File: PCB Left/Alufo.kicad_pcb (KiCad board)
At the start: 2 copper layers, 282.6 x 90.9 mm, 93 parts, among them J1 USB_C_Receptacle_USB2.0_16P_2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, J3 USB_C_Receptacle_USB2.0_16P_2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, J5 Shield_Connection, J7 Shield_Connection, K11 PG1350, K12 PG1350, K13 PG1350, K14 PG1350, K15 PG1350, K16 PG1350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

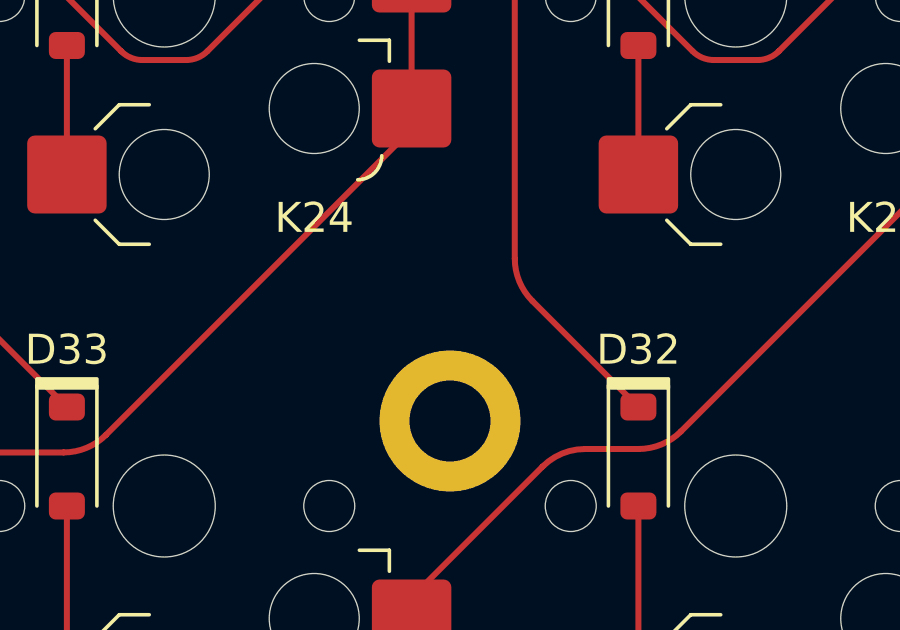
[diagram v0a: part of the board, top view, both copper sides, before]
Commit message: Add shield connection to H3 (lower middle mounting hole)
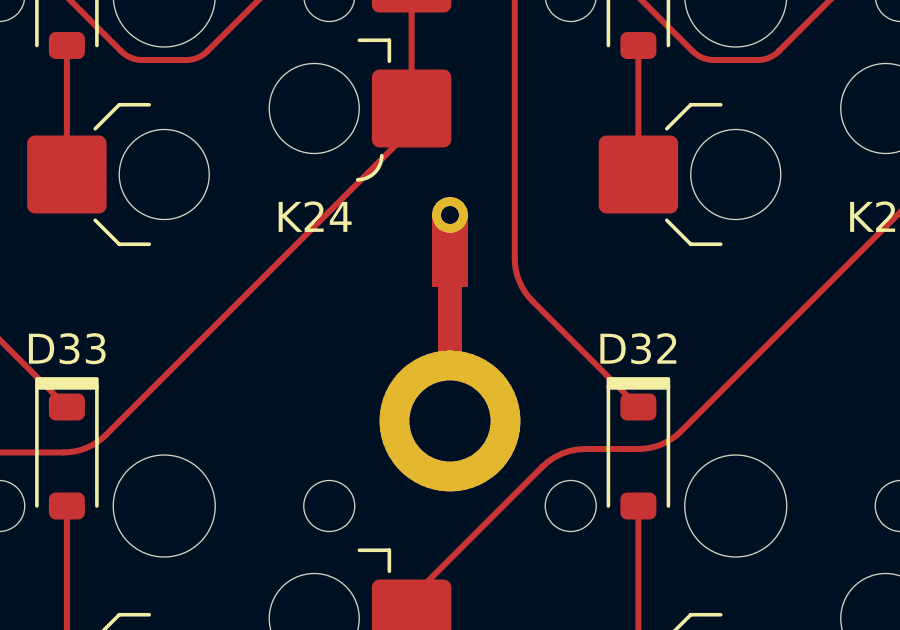
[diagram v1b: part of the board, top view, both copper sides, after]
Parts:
- added J9: Shield_Connection, Project_Library:Shield_Connector, F.Cu at (238.1, 64.9)
- H3: footprint Project_Library:MountingHole_2.2mm_M2_SMD_Solder_Nut -> Project_Library:MountingHole_2.2mm_M2_SMD_Solder_Nut_Pad
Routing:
- net Net-(J9-Pin_1): track 0.00 -> 5.67 mm
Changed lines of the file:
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@@
 	(net 68 "unconnected-(J3-SHIELD-PadS3)")
 	(net 69 "VCC'")
+	(net 70 "Net-(J9-Pin_1)")
 	(footprint "Project_Library:SW_choc_v1_HS_CPG135001S30_1layer_1u"
 		(layer "F.Cu")
@@
 		)
 	)
-	(footprint "Project_Library:MountingHole_2.2mm_M2_SMD_Solder_Nut"
+	(footprint "Project_Library:MountingHole_2.2mm_M2_SMD_Solder_Nut_Pad"
 		(layer "F.Cu")
 		(at 238.125 70.83335)
@@
 			)
 		)
-		(property "Description" "Mounting Hole without connection"
+		(property "Description" "Mounting Hole with connection"
 			(at 0 0 0)
 			(unlocked yes)
@@
 			)
 		)
-		(property ki_fp_filters "MountingHole*")
+		(property ki_fp_filters "MountingHole*Pad*")
 		(sheetname "/")
 		(sheetfile "Alufo.kicad_sch")
@@
 		(fp_circle
 			(center 0 0)
-			(end 3.35 0)
+			(end 2.5 0)
 			(stroke
 				(width 0.1)
@@
 			)
 		)
-		(pad "" thru_hole circle
+		(pad "1" thru_hole circle
 			(at 0 0)
 			(size 4.7 4.7)
@@
 			(layers "*.Cu" "F.Mask")
 			(remove_unused_layers no)
+			(net 70 "Net-(J9-Pin_1)")
+			(pinfunction "1")
+			(pintype "input")
 		)
 		(embedded_fonts no)
@@
 		(embedded_fonts no)
 	)
+	(footprint "Project_Library:Shield_Connector"
+		(layer "F.Cu")
+		(at 238.125 64.866682 180)
+		(descr "Wire connection from PCB to aluminum core")
+		(property "Reference" "J9"
+			(at 0 -0.499999 180)
+			(unlocked yes)
+			(layer "F.SilkS")
+			(hide yes)
+			(effects
+				(font
+					(size 1 1)
+					(thickness 0.1)
+				)
+			)
+		)
+		(property "Value" "Shield_Connection"
+			(at 0 1 180)
+			(unlocked yes)
+			(layer "F.Fab")
+			(effects
+				(font
+					(size 1 1)
+					(thickness 0.15)
+				)
+			)
+		)
+		(property "Datasheet" ""
+			(at 0 0 180)
+			(unlocked yes)
+			(layer "F.Fab")
+			(hide yes)
+			(effects
+				(font
+					(size 1 1)
+					(thickness 0.15)
+				)
+			)
+		)
+		(property "Description" "Generic connector, single row, 01x01, script generated (kicad-library-utils/schlib/autogen/connector/)"
+			(at 0 0 180)
+			(unlocked yes)
+			(layer "F.Fab")
+			(hide yes)
+			(effects
+				(font
+					(size 1 1)
+					(thickness 0.15)
+				)
+			)
+		)
+		(property ki_fp_filters "Connector*:*_1x??_*")
+		(sheetname "/")
+		(sheetfile "Alufo.kicad_sch")
+		(attr smd)
+		(fp_poly
+			(pts
+				(arc
+					(start -0.4 -1.8)
+					(mid -0.753553 -1.653553)
+					(end -0.9 -1.3)
+				)
+				(arc
+					(start -0.9 0.9)
+					(mid -0.636396 1.536396)
+					(end 0 1.8)
+				)
+				(arc
+					(start 0 1.8)
+					(mid 0.636396 1.536396)
+					(end 0.9 0.9)
+				)
+				(arc
+					(start 0.9 -1.3)
+					(mid 0.753553 -1.653553)
+					(end 0.4 -1.8)
+				)
+			)
+			(stroke
+				(width 0.1)
+				(type solid)
+			)
+			(fill no)
+			(layer "User.3")
+		)
+		(fp_text user "${REFERENCE}"
+			(at 0 2.5 180)
+			(unlocked yes)
+			(layer "F.Fab")
+			(effects
+				(font
+					(size 1 1)
+					(thickness 0.15)
+				)
+			)
+		)
+		(pad "1" smd roundrect
+			(at 0 -0.3 180)
+			(size 1.2 2.4)
+			(layers "F.Cu" "F.Mask" "F.Paste")
+			(roundrect_rratio 0.2)
+			(chamfer_ratio 0)
+			(chamfer bottom_left bottom_right)
+			(net 70 "Net-(J9-Pin_1)")
+			(pinfunction "Pin_1")
+			(pintype "passive")
+			(thermal_bridge_angle 45)
+		)
+		(pad "1" thru_hole circle
+			(at 0 0.9 180)
+			(size 1.2 1.2)
+			(drill 0.6)
+			(layers "*.Cu" "*.Paste" "*.Mask")
+			(remove_unused_layers no)
+			(net 70 "Net-(J9-Pin_1)")
+			(pinfunction "Pin_1")
+			(pintype "passive")
+		)
+		(embedded_fonts no)
+	)
 	(footprint "BGK_Kicad:D_SOD-323"
 		(layer "F.Cu")
@@
 		(net 69)
 	)
+	(segment
+		(start 238.125 65.166682)
+		(end 238.125 70.83335)
+		(width 0.8)
+		(layer "F.Cu")
+		(net 70)
+	)
 	(zone

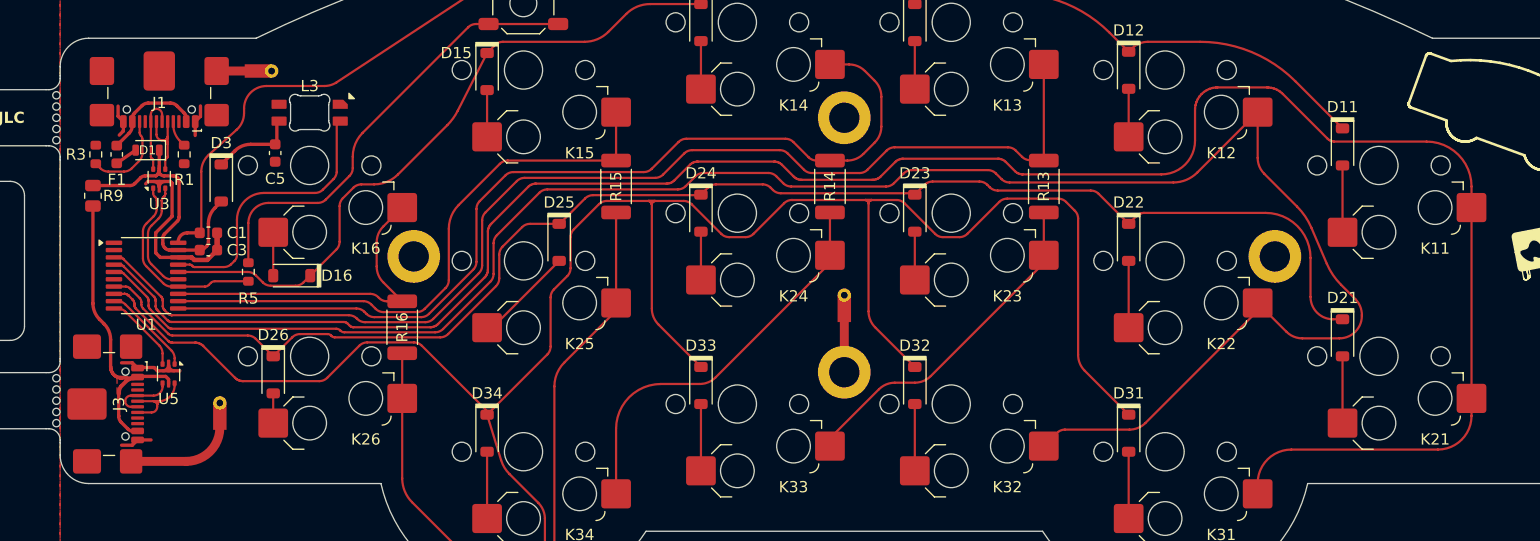
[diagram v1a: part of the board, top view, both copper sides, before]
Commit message: Move split ports to give adequate clearance for SMD legs
Also:

 * Ensure that split ports are aligned with PCB edge,
 * Set hole size for shield connector to 0.65mm, JLC’s minimum hole size on aluminium boards, and
 * Remove back mask and paste from shield connector — these won’t be included in the production files, but trigger a DRC warning on one of the instances.
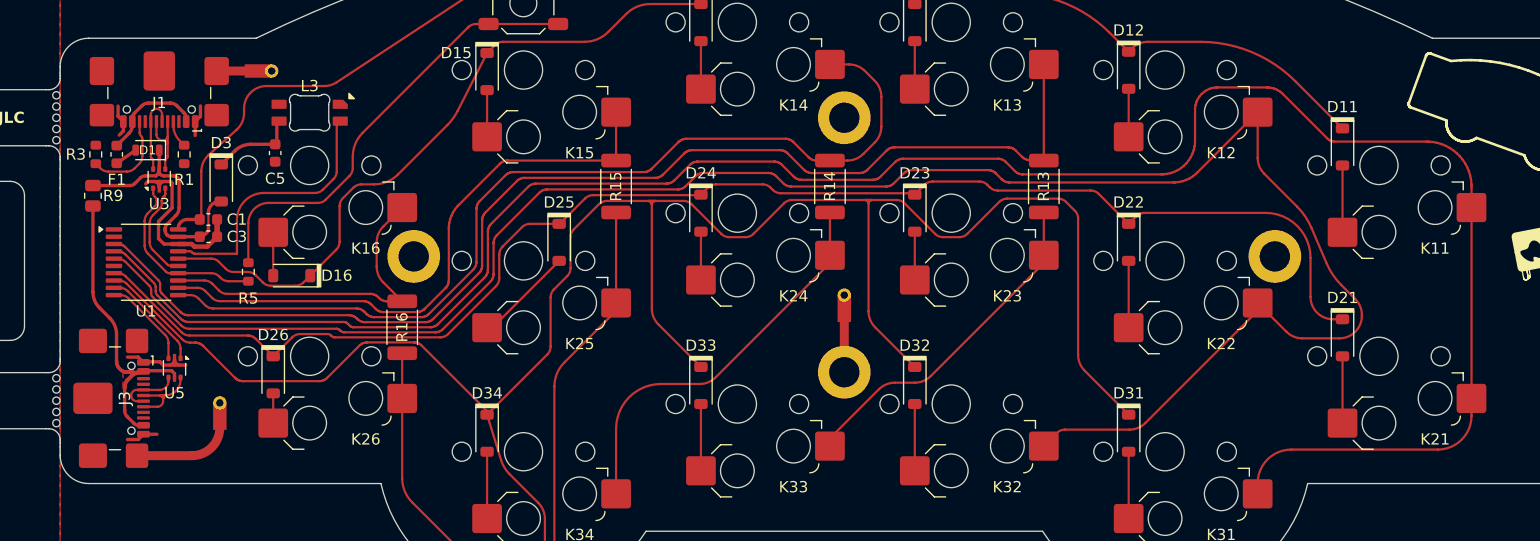
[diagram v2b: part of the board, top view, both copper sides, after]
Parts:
- moved C1 1.19 mm to (181.5, 57.2)
- moved C3 1.19 mm to (181.5, 58.8)
- moved U1 1.19 mm to (175.9, 61.0)
- moved J3 0.73 mm to (172.0, 73.2)
- moved U5 0.73 mm to (178.5, 70.4)
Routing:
- net VCC: track 25.3 -> 22.7 mm
- net GND: track 26.7 -> 25.1 mm
- net USB-: track 9.62 -> 8.23 mm
- net +3V3: track 72.1 -> 70.9 mm
- net TX: track 7.86 -> 8.67 mm
- net RX: track 6.76 -> 7.54 mm
- net Col2: track 172.0 -> 172.7 mm
- net LED: track 24.7 -> 24.0 mm
- net USB+: track 16.6 -> 15.9 mm
- net Col1: track 185.3 -> 185.9 mm
